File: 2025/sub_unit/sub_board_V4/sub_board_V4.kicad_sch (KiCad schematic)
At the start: 29 parts, among them J1 Conn_01x02_Socket, J10 Conn_01x02_Socket, J11 Conn_01x03_Socket, J12 Conn_01x02_Socket, J13 Conn_01x02_Socket, J14 Conn_01x05_Socket, J15 Conn_01x05_Socket, J16 Conn_01x02_Socket, J18 Conn_01x07_Socket, J19 Conn_01x07_Socket, J2 Conn_01x02_Socket, J3 Conn_01x02_Socket, J4 Conn_01x02_Socket, J5 Conn_01x02_Socket, J6 Conn_01x02_Socket, J7 Conn_01x02_Socket, J8 Conn_01x02_Socket, J9 Conn_01x02_Socket

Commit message: 回路図変更
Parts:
- added J17: Conn_01x02_Socket, Connector_JST:JST_PH_B2B-PH-K_1x02_P2.00mm_Vertical, symbol Connector:Conn_01x02_Socket
- J11: footprint (none) -> Connector_Molex:Molex_SPOX_5267-03A_1x03_P2.50mm_Vertical
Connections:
- net +6V: now also J11.3 (Pin_3)
- net CANH: now also J17.2 (Pin_2)
- net CANL: now also J17.1 (Pin_1)
- net DRI_SIGNAL: no longer names the net of J19.3 (Pin_3)
- no-connect marks 0 -> 1
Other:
- moved on the sheet: J1, J2, J3, J4

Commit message: PCB修正
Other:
- moved on the sheet: C1, C2, C3, C4, D2, J1, J12, J13, J14, J15, J16, J17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

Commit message: PCB修正2
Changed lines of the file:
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@@
 	(text_box "PHOTO"
 		(exclude_from_sim no)
-		(at 13.97 208.28 0)
+		(at 16.51 130.81 0)
 		(size 156.718 64.77)
 		(stroke
@@
 	(text_box "POWER"
 		(exclude_from_sim no)
-		(at -78.74 12.7 0)
-		(size 87.63 111.506)
+		(at 16.51 13.97 0)
+		(size 87.63 115.316)
 		(stroke
 			(width 0)

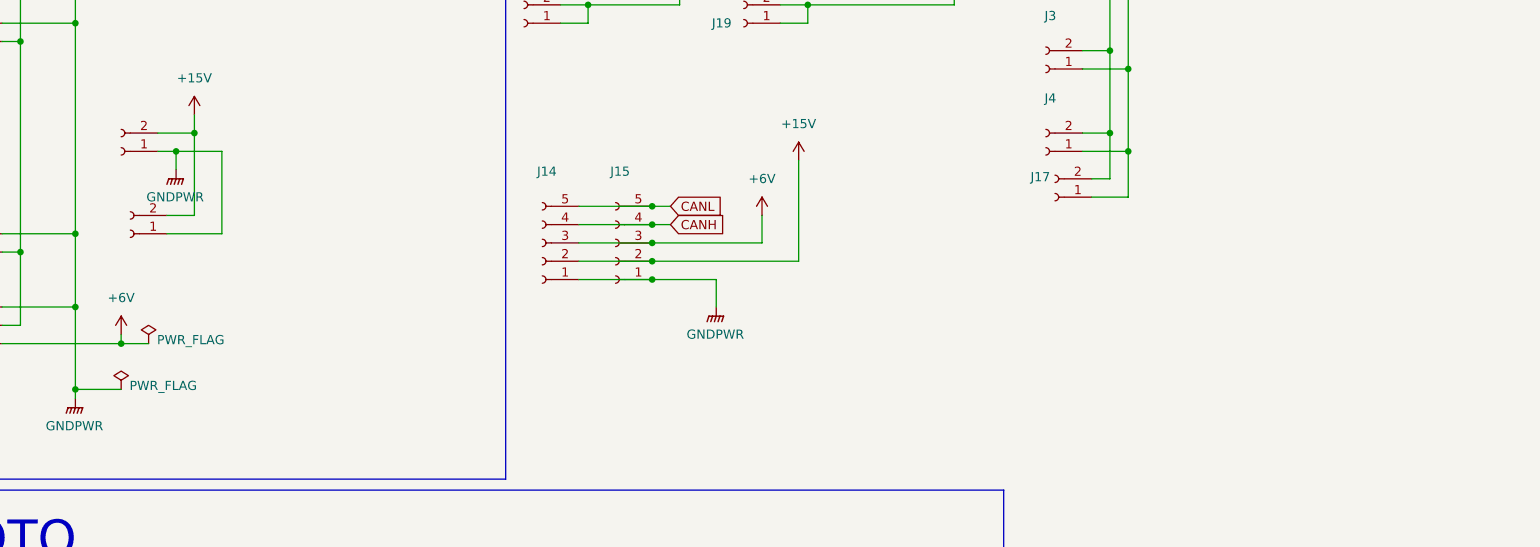
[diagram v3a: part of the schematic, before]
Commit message: 完成、製造データ出力
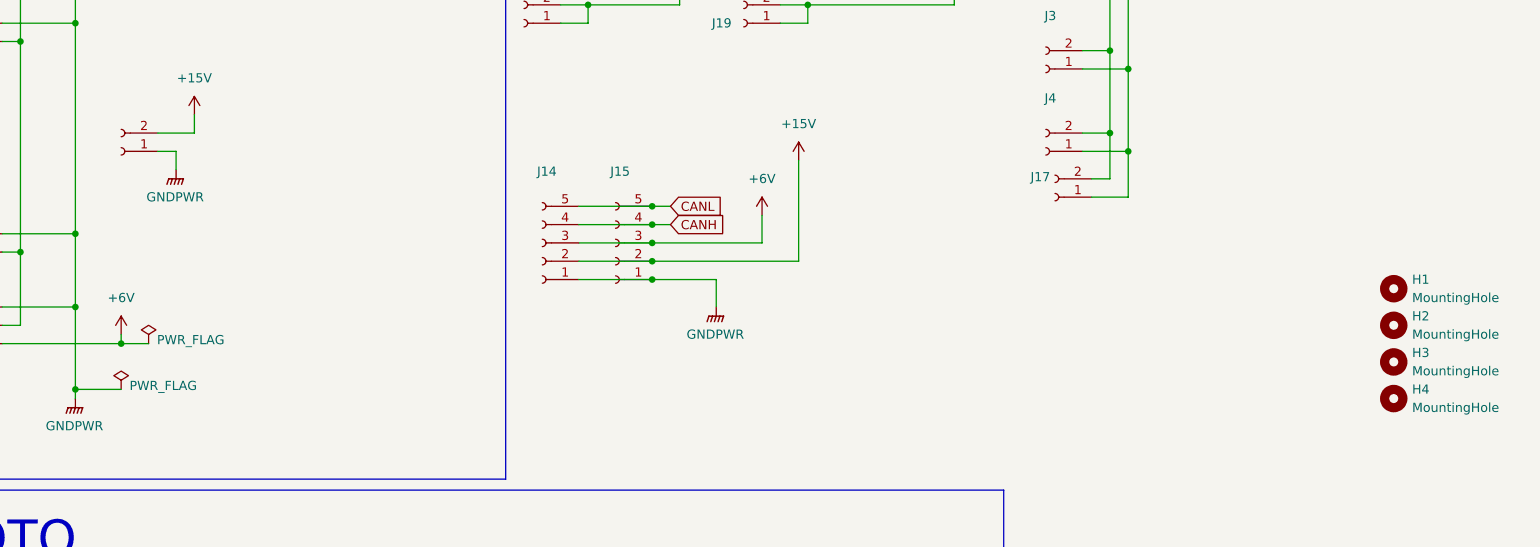
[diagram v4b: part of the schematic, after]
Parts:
- removed J9: Conn_01x02_Socket, Connector_AMASS:AMASS_XT30UPB-M_1x02_P5.0mm_Vertical, symbol Connector:Conn_01x02_Socket
- added H1, H2, H3, H4: MountingHole, MountingHole:MountingHole_2.2mm_M2_DIN965_Pad, symbol Mechanical:MountingHole

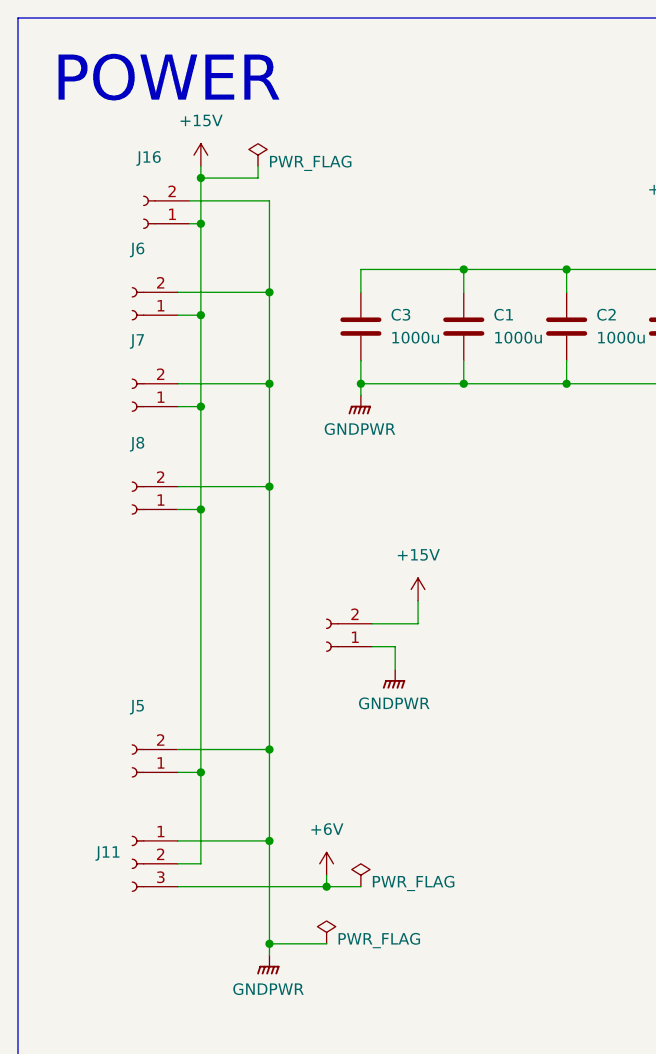
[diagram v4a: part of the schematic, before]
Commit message: ドリブラー用コネクタのピン配置変更
製造データ再出力
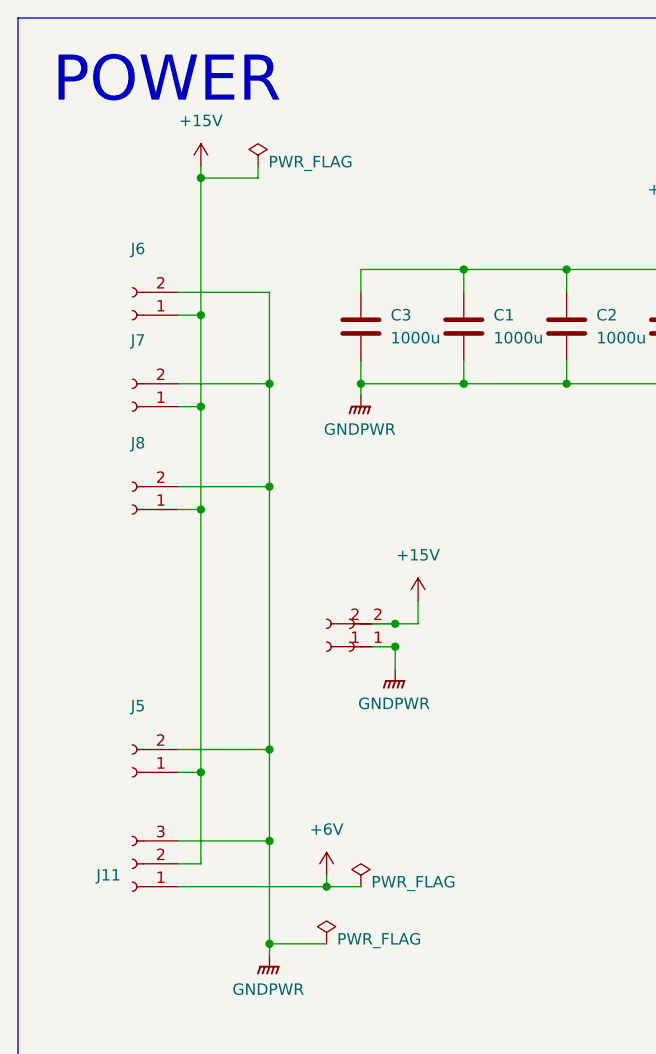
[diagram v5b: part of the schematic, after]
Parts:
- removed J16: Conn_01x02_Socket, Connector_Molex:Molex_SPOX_5267-02A_1x02_P2.50mm_Vertical, symbol Connector:Conn_01x02_Socket
- added J9: Conn_01x02_Socket, Connector_AMASS:AMASS_XT30UPB-M_1x02_P5.0mm_Vertical, symbol Connector:Conn_01x02_Socket
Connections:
- net +15V: now also J9.2 (Pin_2)
- net +6V: now also J11.1 (Pin_1); no longer J11.3 (Pin_3)
- net GNDPWR: now also J11.3 (Pin_3), J9.1 (Pin_1); no longer J11.1 (Pin_1)
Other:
- moved on the sheet: J11
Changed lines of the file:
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@@
 	)
 	(junction
-		(at 36.83 36.83)
-		(diameter 0)
-		(color 0 0 0 0)
-	)
-	(junction
 		(at 36.83 46.99)
 		(diameter 0)
@@
 	)
 	(junction
+		(at 58.42 83.82)
+		(diameter 0)
+		(color 0 0 0 0)
+	)
+	(junction
 		(at 44.45 105.41)
 		(diameter 0)
@@
 	)
 	(junction
-		(at 44.45 44.45)
+		(at 58.42 81.28)
 		(diameter 0)
 		(color 0 0 0 0)
@@
 	(wire
 		(pts
-			(xy 35.56 36.83) (xy 36.83 36.83)
-		)
-		(stroke
-			(width 0)
-			(type default)
-		)
-	)
-	(wire
-		(pts
 			(xy 187.96 87.63) (xy 187.96 81.28)
 		)
@@
 	(wire
 		(pts
-			(xy 36.83 36.83) (xy 36.83 46.99)
-		)
-		(stroke
-			(width 0)
-			(type default)
-		)
-	)
-	(wire
-		(pts
 			(xy 128.27 62.23) (xy 128.27 63.5)
 		)
@@
 	(wire
 		(pts
-			(xy 44.45 34.29) (xy 44.45 44.45)
-		)
-		(stroke
-			(width 0)
-			(type default)
-		)
-	)
-	(wire
-		(pts
 			(xy 185.42 90.17) (xy 190.5 90.17)
 		)
@@
 	(wire
 		(pts
-			(xy 36.83 31.75) (xy 36.83 36.83)
+			(xy 58.42 81.28) (xy 60.96 81.28)
 		)
 		(stroke
@@
 	(wire
 		(pts
-			(xy 190.5 62.23) (xy 190.5 72.39)
+			(xy 36.83 31.75) (xy 36.83 46.99)
 		)
 		(stroke
@@
 	(wire
 		(pts
-			(xy 146.05 53.34) (xy 161.29 53.34)
+			(xy 190.5 62.23) (xy 190.5 72.39)
 		)
 		(stroke
@@
 	(wire
 		(pts
-			(xy 44.45 34.29) (xy 35.56 34.29)
+			(xy 146.05 53.34) (xy 161.29 53.34)
 		)
 		(stroke
@@
 	(wire
 		(pts
-			(xy 55.88 81.28) (xy 60.96 81.28)
+			(xy 55.88 81.28) (xy 58.42 81.28)
 		)
 		(stroke
@@
 	(symbol
 		(lib_id "Connector:Conn_01x03_Socket")
-		(at 29.21 107.95 0)
-		(mirror y)
+		(at 29.21 107.95 180)
 		(unit 1)
 		(exclude_from_sim no)
@@
 		(dnp no)
 		(property "Reference" "J11"
-			(at 27.94 106.6799 0)
+			(at 27.94 109.2201 0)
 			(effects
 				(font
@@
 		)
 		(property "Value" "Conn_01x03_Socket"
-			(at 27.94 109.2199 0)
+			(at 27.94 106.6801 0)
 			(effects
 				(font
@@
 	)
 	(symbol
-		(lib_id "Connector:Conn_01x02_Socket")
-		(at 30.48 36.83 180)
-		(unit 1)
-		(exclude_from_sim no)
-		(in_bom yes)
-		(on_board yes)
-		(dnp no)
-		(fields_autoplaced yes)
-		(property "Reference" "J16"
-			(at 31.115 29.464 0)
-			(effects
-				(font
-					(size 1.27 1.27)
-				)
-			)
-		)
-		(property "Value" "Conn_01x02_Socket"
-			(at 31.115 32.004 0)
-			(effects
-				(font
-					(size 1.27 1.27)
-				)
-				(hide yes)
-			)
-		)
-		(property "Footprint" "Connector_Molex:Molex_SPOX_5267-02A_1x02_P2.50mm_Vertical"
-			(at 30.48 36.83 0)
-			(effects
-				(font
-					(size 1.27 1.27)
-				)
-				(hide yes)
-			)
-		)
-		(property "Datasheet" "~"
-			(at 30.48 36.83 0)
-			(effects
-				(font
-					(size 1.27 1.27)
-				)
-				(hide yes)
-			)
-		)
-		(property "Description" ""
-			(at 30.48 36.83 0)
-			(effects
-				(font
-					(size 1.27 1.27)
-				)
-				(hide yes)
-			)
-		)
-		(pin "1"
-		)
-		(pin "2"
-		)
-		(instances
-			(project "sub_board_V4"
-				(path "/f588d83c-66c1-45ba-96cd-d938f5aa02a1"
-					(reference "J16")
-					(unit 1)
-				)
-			)
-		)
-	)
-	(symbol
 		(lib_name "GNDPWR_1")
 		(lib_id "power:GNDPWR")
@@
 					(unit 1)
 				)
+			)
+		)
+	)
+	(symbol
+		(lib_id "Connector:Conn_01x02_Socket")
+		(at 53.34 83.82 180)
+		(unit 1)
+		(exclude_from_sim no)
+		(in_bom yes)
+		(on_board yes)
+		(dnp no)
+		(property "Reference" "J9"
+			(at 53.975 76.454 0)
+			(effects
+				(font
+					(size 1.27 1.27)
+				)
+				(hide yes)
+			)
+		)
+		(property "Value" "Conn_01x02_Socket"
+			(at 53.975 78.994 0)
+			(effects
+				(font
+					(size 1.27 1.27)
+				)
+				(hide yes)
+			)
+		)
+		(property "Footprint" "Connector_AMASS:AMASS_XT30UPB-M_1x02_P5.0mm_Vertical"
+			(at 53.34 83.82 0)
+			(effects
+				(font
+					(size 1.27 1.27)
+				)
+				(hide yes)
+			)
+		)
+		(property "Datasheet" "~"
+			(at 53.34 83.82 0)
+			(effects
+				(font
+					(size 1.27 1.27)
+				)
+				(hide yes)
+			)
+		)
+		(property "Description" ""
+			(at 53.34 83.82 0)
+			(effects
+				(font
+					(size 1.27 1.27)
+				)
+				(hide yes)
+			)
+		)
+		(pin "1"
+		)
+		(pin "2"
+		)
+		(instances
+			(project "sub_board_V4"
+				(path "/f588d83c-66c1-45ba-96cd-d938f5aa02a1"
+					(reference "J9")
+					(unit 1)
+				)

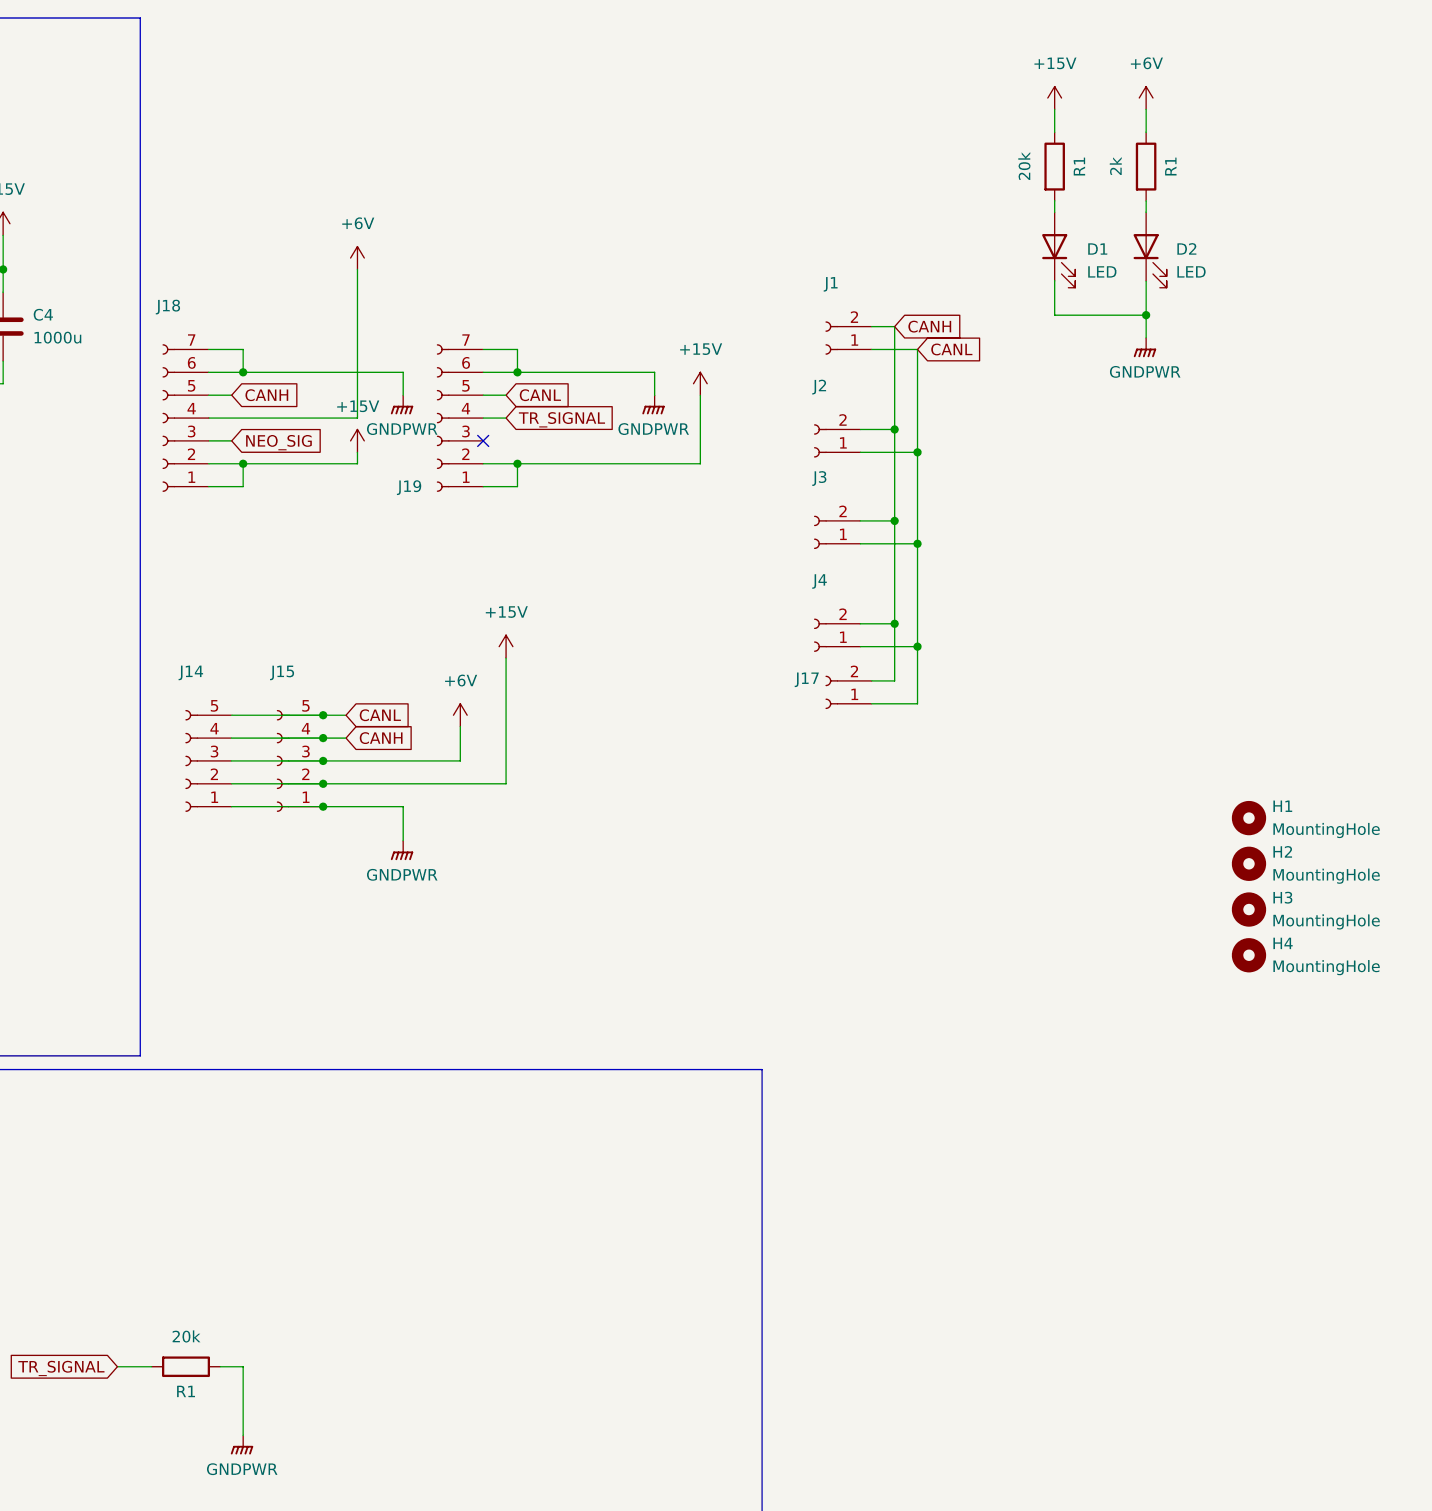
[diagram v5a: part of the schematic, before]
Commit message: 抵抗値の変更、ibomの生成
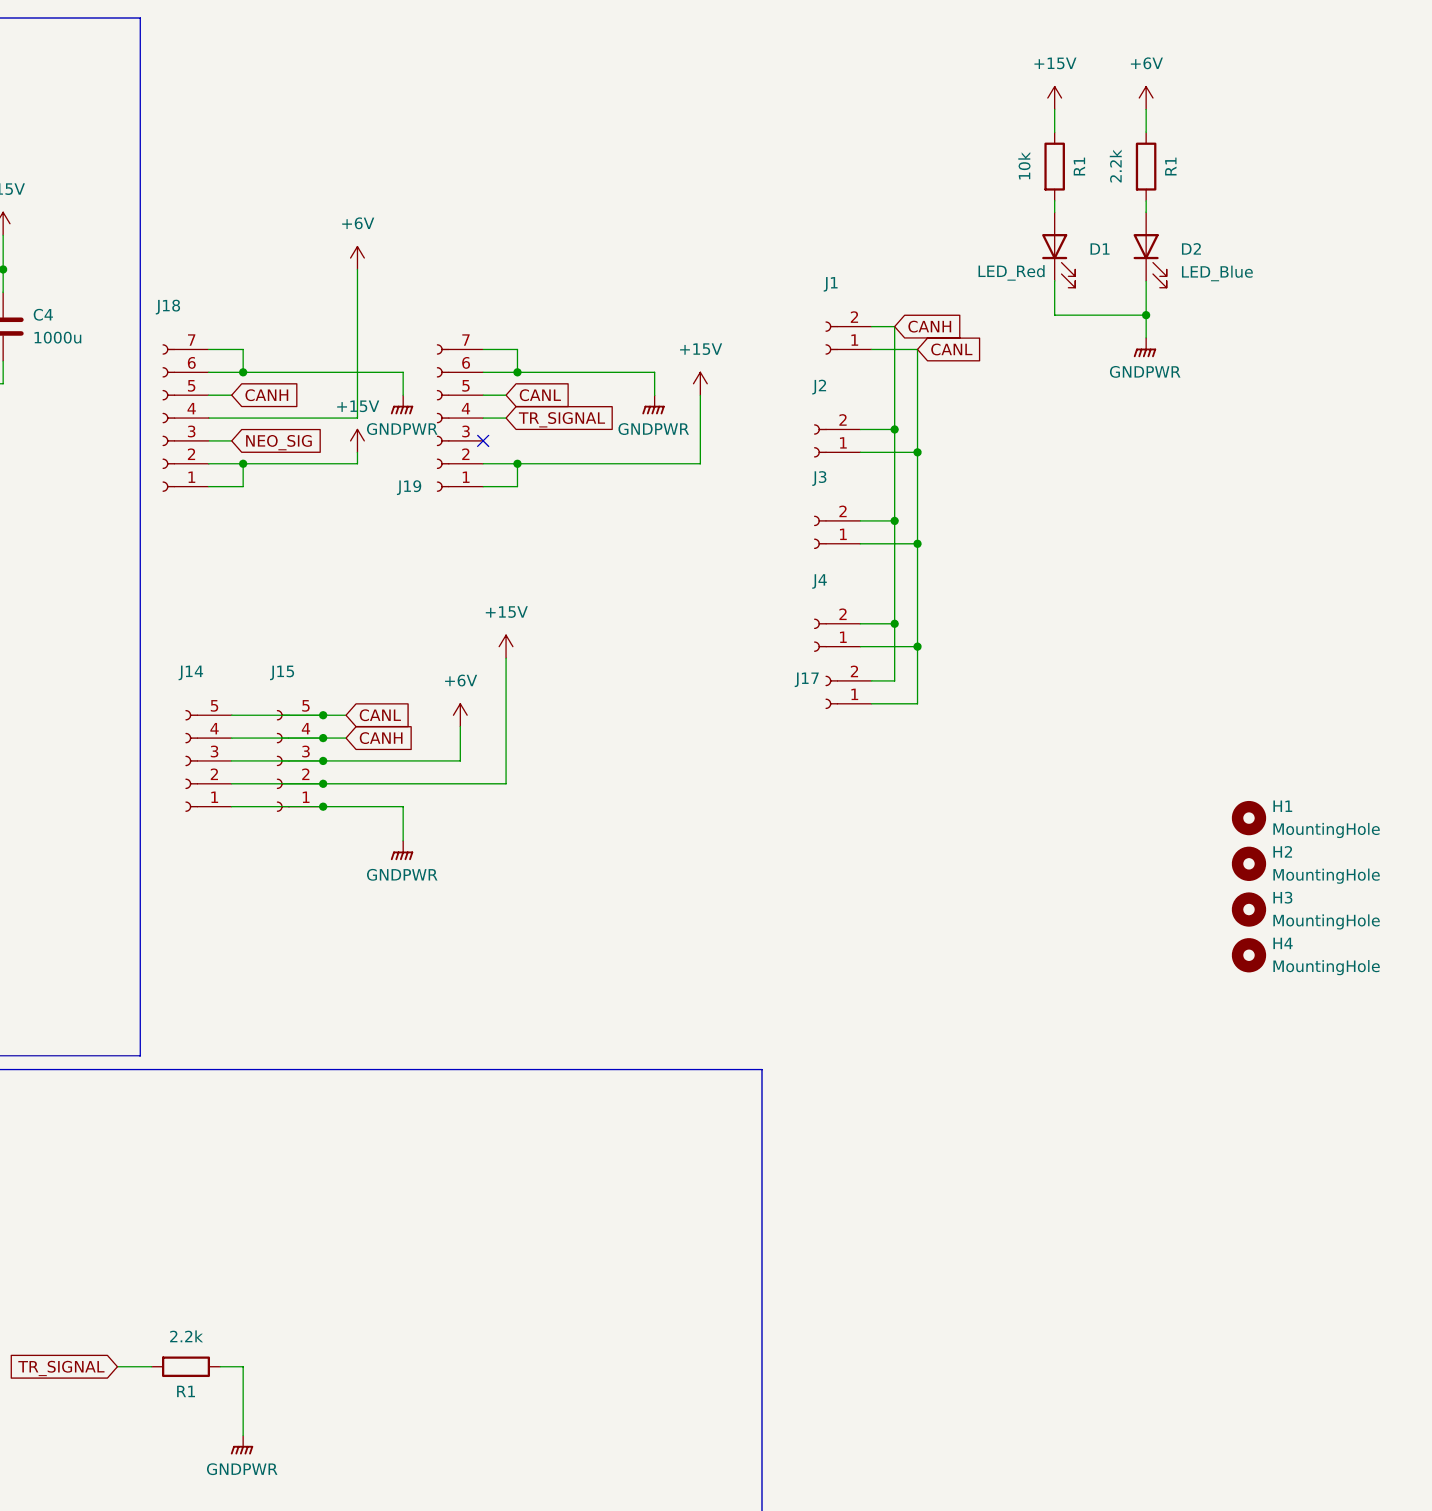
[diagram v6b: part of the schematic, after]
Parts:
- D1: value LED -> LED_Red
- D2: value LED -> LED_Blue
- R1: value 20k -> 10k
- R1: value 20k -> 2.2k
- R1: value 2k -> 2.2k
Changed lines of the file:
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@@
 			)
 		)
-		(property "Value" "20k"
+		(property "Value" "10k"
 			(at 202.438 30.48 90)
 			(effects
@@
 			)
 		)
-		(property "Value" "20k"
+		(property "Value" "2.2k"
 			(at 109.22 160.528 90)
 			(effects
@@
 		(on_board yes)
 		(dnp no)
-		(fields_autoplaced yes)
 		(property "Reference" "D1"
-			(at 209.296 39.6875 90)
+			(at 209.55 39.6874 90)
 			(effects
 				(font
@@
 			)
 		)
-		(property "Value" "LED"
-			(at 209.296 42.2275 90)
+		(property "Value" "LED_Red"
+			(at 197.104 42.164 90)
 			(effects
 				(font
@@
 		(fields_autoplaced yes)
 		(property "Reference" "D2"
-			(at 219.202 39.6875 90)
+			(at 219.71 39.6874 90)
 			(effects
 				(font
@@
 			)
 		)
-		(property "Value" "LED"
-			(at 219.202 42.2275 90)
+		(property "Value" "LED_Blue"
+			(at 219.71 42.2274 90)
 			(effects
 				(font
@@
 			)
 		)
-		(property "Value" "2k"
+		(property "Value" "2.2k"
 			(at 212.598 30.48 90)
 			(effects
